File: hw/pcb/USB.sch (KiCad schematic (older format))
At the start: 9 parts, among them J301 USB_B_Micro, Q301 SS8050-G, Q302 SS8050-G, U301 CP2102N-A01-GQFN28

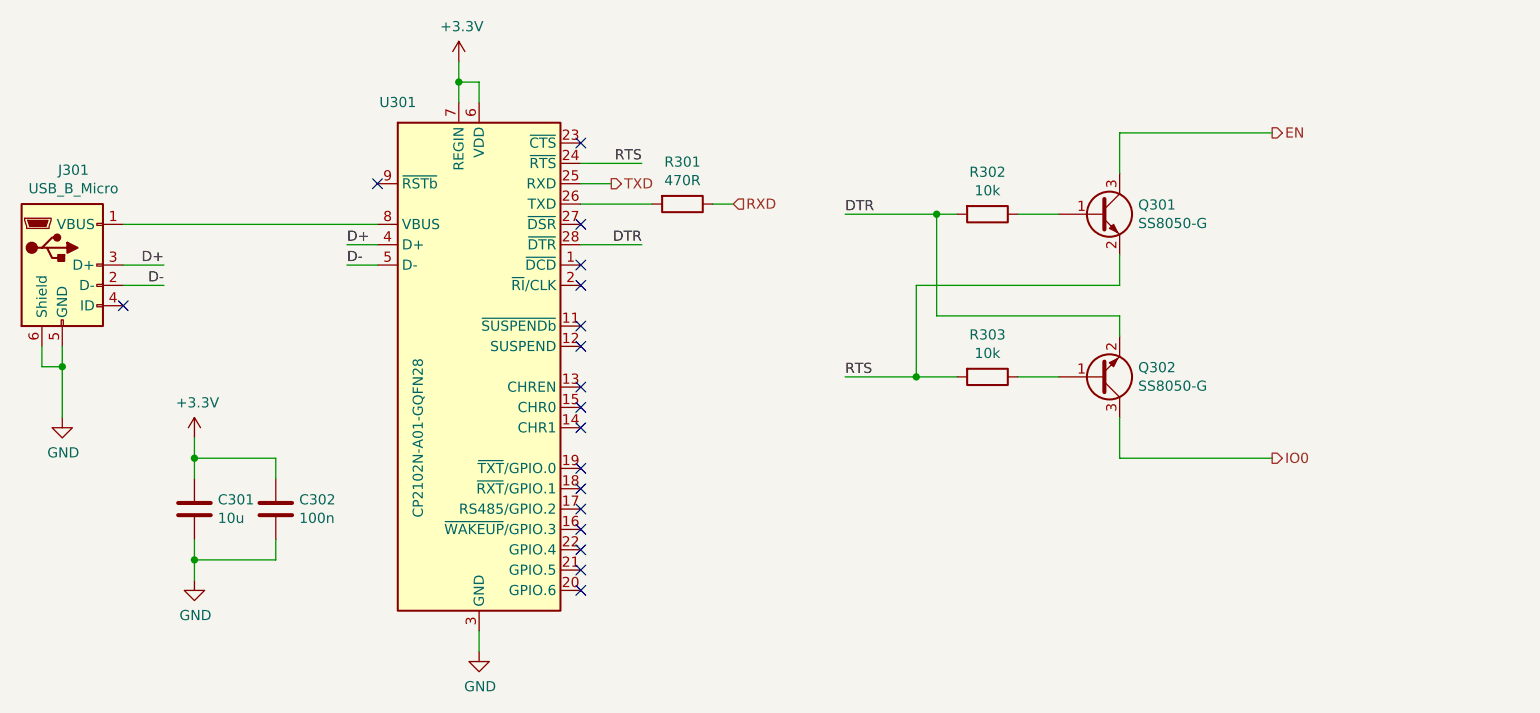
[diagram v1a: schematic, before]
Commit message: fixed severe PCB issue, clearance of ground fills was too small, could lead to thermal instability
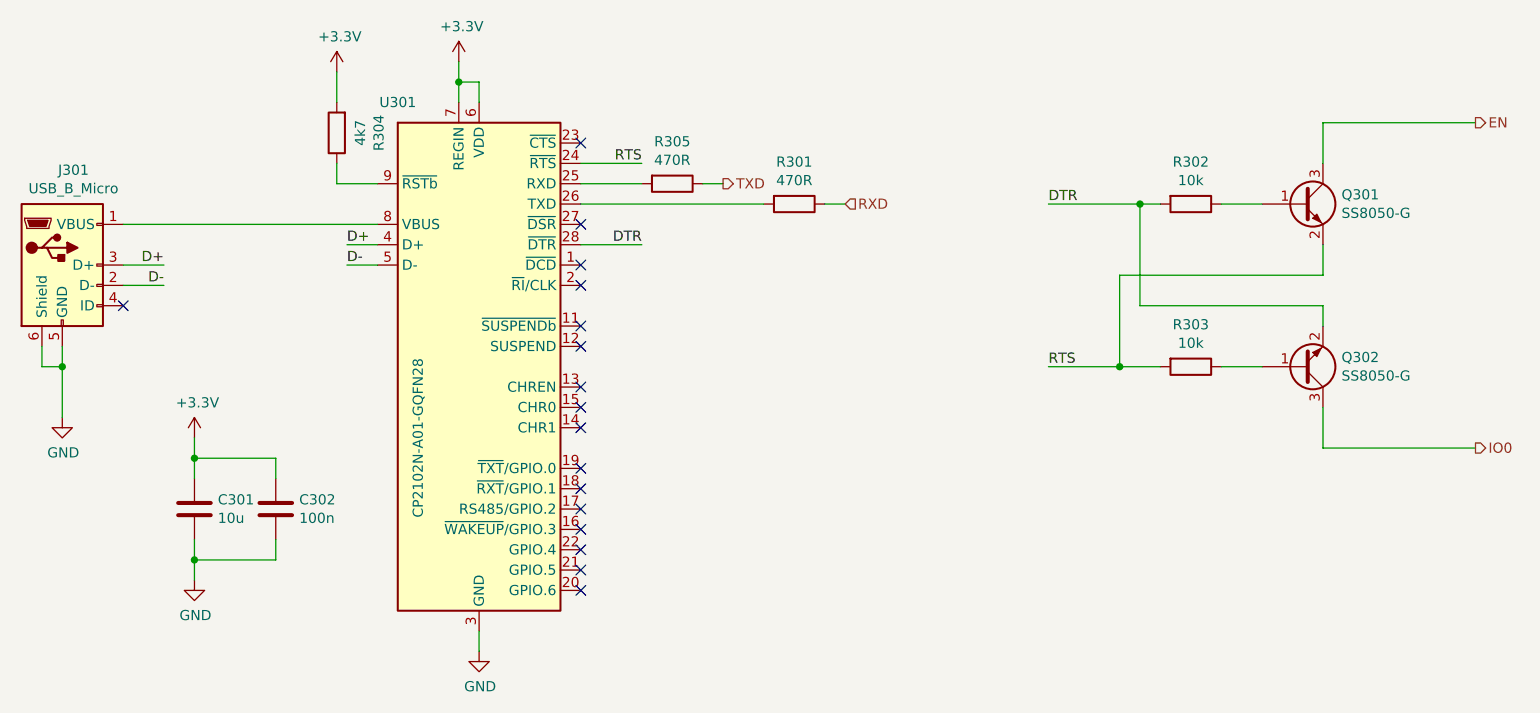
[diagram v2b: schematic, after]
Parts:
- added R304: 4k7, Resistor_SMD:R_0402_1005Metric, symbol Device:R
- added R305: 470R, Resistor_SMD:R_0402_1005Metric, symbol Device:R
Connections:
- net +3V3: now also R304.2
- net TXD: now also R305.1; no longer U301.25 (RXD)
- net at U301.9 (~RSTb): now also R304.1
- new net: R305.2, U301.25 (RXD)
- no-connect marks 18 -> 17
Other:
- moved on the sheet: Q301, Q302, R301, R302, R303
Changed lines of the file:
@@
 encoding utf-8
 Sheet 3 6
-Title "CTAG-TBD"
-Date "2020-06-06"
-Rev "C"
+Title "ESP32 Eurorack Audio Module"
+Date "2020-08-18"
+Rev "G"
 Comp "(c) Robert Manzke 2020"
 Comment1 "https://creativecommons.org/licenses/by-nc-sa/4.0/"
@@
 L Device:Q_NPN_BEC Q?
 U 1 1 5B81BF2F
-P 8150 1650
+P 9150 1600
 AR Path="/5B66F258/5B81BF2F" Ref="Q?"  Part="1"
 AR Path="/5B81850F/5B81BF2F" Ref="Q301"  Part="1"
-F 0 "Q301" H 8341 1696 50  0000 L CNN
-F 1 "SS8050-G" H 8341 1605 50  0000 L CNN
-F 2 "Package_TO_SOT_SMD:SOT-23" H 8350 1750 50  0001 C CNN
-F 3 "~" H 8150 1650 50  0001 C CNN
-	1    8150 1650
+F 0 "Q301" H 9341 1646 50  0000 L CNN
+F 1 "SS8050-G" H 9341 1555 50  0000 L CNN
+F 2 "Package_TO_SOT_SMD:SOT-23" H 9350 1700 50  0001 C CNN
+F 3 "~" H 9150 1600 50  0001 C CNN
+	1    9150 1600
 	1    0    0    -1
 $EndComp
@@
 L Device:Q_NPN_BEC Q?
 U 1 1 5B81BF36
-P 8150 2450
+P 9150 2400
 AR Path="/5B66F258/5B81BF36" Ref="Q?"  Part="1"
 AR Path="/5B81850F/5B81BF36" Ref="Q302"  Part="1"
-F 0 "Q302" H 8341 2404 50  0000 L CNN
-F 1 "SS8050-G" H 8341 2495 50  0000 L CNN
-F 2 "Package_TO_SOT_SMD:SOT-23" H 8350 2550 50  0001 C CNN
-F 3 "~" H 8150 2450 50  0001 C CNN
-	1    8150 2450
+F 0 "Q302" H 9341 2354 50  0000 L CNN
+F 1 "SS8050-G" H 9341 2445 50  0000 L CNN
+F 2 "Package_TO_SOT_SMD:SOT-23" H 9350 2500 50  0001 C CNN
+F 3 "~" H 9150 2400 50  0001 C CNN
+	1    9150 2400
 	1    0    0    1
 $EndComp
@@
 L Device:R R?
 U 1 1 5B81BF3D
-P 7600 1650
+P 8600 1600
 AR Path="/5B66F258/5B81BF3D" Ref="R?"  Part="1"
 AR Path="/5B81850F/5B81BF3D" Ref="R302"  Part="1"
-F 0 "R302" V 7393 1650 50  0000 C CNN
-F 1 "10k" V 7484 1650 50  0000 C CNN
-F 2 "Resistor_SMD:R_0402_1005Metric" V 7530 1650 50  0001 C CNN
-F 3 "~" H 7600 1650 50  0001 C CNN
-	1    7600 1650
+F 0 "R302" V 8393 1600 50  0000 C CNN
+F 1 "10k" V 8484 1600 50  0000 C CNN
+F 2 "Resistor_SMD:R_0402_1005Metric" V 8530 1600 50  0001 C CNN
+F 3 "~" H 8600 1600 50  0001 C CNN
+	1    8600 1600
 	0    1    1    0
 $EndComp
@@
 L Device:R R?
 U 1 1 5B81BF44
-P 7600 2450
+P 8600 2400
 AR Path="/5B66F258/5B81BF44" Ref="R?"  Part="1"
 AR Path="/5B81850F/5B81BF44" Ref="R303"  Part="1"
-F 0 "R303" V 7393 2450 50  0000 C CNN
-F 1 "10k" V 7484 2450 50  0000 C CNN
-F 2 "Resistor_SMD:R_0402_1005Metric" V 7530 2450 50  0001 C CNN
-F 3 "~" H 7600 2450 50  0001 C CNN
-	1    7600 2450
+F 0 "R303" V 8393 2400 50  0000 C CNN
+F 1 "10k" V 8484 2400 50  0000 C CNN
+F 2 "Resistor_SMD:R_0402_1005Metric" V 8530 2400 50  0001 C CNN
+F 3 "~" H 8600 2400 50  0001 C CNN
+	1    8600 2400
 	0    1    1    0
 $EndComp
 Wire Wire Line
-	7950 1650 7750 1650
-Wire Wire Line
-	7950 2450 7750 2450
-Wire Wire Line
-	8250 1850 8250 2000
-Wire Wire Line
-	8250 2000 7250 2000
-Wire Wire Line
-	7250 2000 7250 2450
-Wire Wire Line
-	7250 2450 7450 2450
-Wire Wire Line
-	8250 2250 8250 2150
-Wire Wire Line
-	7350 2150 7350 1650
-Wire Wire Line
-	7350 1650 7450 1650
-Wire Wire Line
-	8250 1250 8250 1450
-Wire Wire Line
-	8250 2650 8250 2850
-Connection ~ 7350 1650
-Wire Wire Line
-	7250 2450 6900 2450
-Connection ~ 7250 2450
-Text Label 6900 1650 0    50   ~ 0
+	8950 1600 8750 1600
+Wire Wire Line
+	8950 2400 8750 2400
+Wire Wire Line
+	9250 1800 9250 1950
+Wire Wire Line
+	9250 1950 8250 1950
+Wire Wire Line
+	8250 1950 8250 2400
+Wire Wire Line
+	8250 2400 8450 2400
+Wire Wire Line
+	9250 2200 9250 2100
+Wire Wire Line
+	8350 2100 8350 1600
+Wire Wire Line
+	8350 1600 8450 1600
+Wire Wire Line
+	9250 1200 9250 1400
+Wire Wire Line
+	9250 2600 9250 2800
+Connection ~ 8350 1600
+Wire Wire Line
+	8250 2400 7900 2400
+Connection ~ 8250 2400
+Text Label 7900 1600 0    50   ~ 0
 DTR
-Text Label 6900 2450 0    50   ~ 0
+Text Label 7900 2400 0    50   ~ 0
 RTS
 $Comp
@@
 Wire Wire Line
 	5600 1800 5900 1800
-Text HLabel 9000 1250 2    50   Output ~ 0
+Text HLabel 10000 1200 2    50   Output ~ 0
 EN
-Text HLabel 9000 2850 2    50   Output ~ 0
+Text HLabel 10000 2800 2    50   Output ~ 0
 IO0
-Text HLabel 5750 1500 2    50   Output ~ 0
+Text HLabel 6300 1500 2    50   Output ~ 0
 TXD
-Text HLabel 6350 1600 2    50   Input ~ 0
+Text HLabel 6900 1600 2    50   Input ~ 0
 RXD
 Wire Wire Line
 	5600 1400 5900 1400
 Wire Wire Line
-	5600 1500 5750 1500
-Wire Wire Line
-	8250 1250 9000 1250
-Wire Wire Line
-	6900 1650 7350 1650
-Wire Wire Line
-	8250 2850 9000 2850
+	9250 1200 10000 1200
+Wire Wire Line
+	7900 1600 8350 1600
+Wire Wire Line
+	9250 2800 10000 2800
 $Comp
 L Device:C C?
@@
 NoConn ~ 5600 3500
 Wire Wire Line
-	7350 2150 8250 2150
+	8350 2100 9250 2100
 NoConn ~ 3350 2100
 Wire Wire Line
@@
 Wire Wire Line
 	3050 2400 3050 2650
-NoConn ~ 4600 1500
 $Comp
 L Device:R R301
 U 1 1 5DBD0908
-P 6100 1600
-F 0 "R301" V 5893 1600 50  0000 C CNN
-F 1 "470R" V 5984 1600 50  0000 C CNN
-F 2 "Resistor_SMD:R_0402_1005Metric" V 6030 1600 50  0001 C CNN
-F 3 "~" H 6100 1600 50  0001 C CNN
-	1    6100 1600
+P 6650 1600
+F 0 "R301" V 6443 1600 50  0000 C CNN
+F 1 "470R" V 6534 1600 50  0000 C CNN
+F 2 "Resistor_SMD:R_0402_1005Metric" V 6580 1600 50  0001 C CNN
+F 3 "~" H 6650 1600 50  0001 C CNN
+	1    6650 1600
 	0    1    1    0
 $EndComp
 Wire Wire Line
-	5950 1600 5600 1600
-Wire Wire Line
-	6250 1600 6350 1600
+	6500 1600 5600 1600
+Wire Wire Line
+	6800 1600 6900 1600
 Wire Wire Line
 	3350 1700 4600 1700
+$Comp
+L Device:R R304
+U 1 1 5F132412
+P 4400 1250
+F 0 "R304" V 4193 1250 50  0000 C CNN
+F 1 "4k7" V 4284 1250 50  0000 C CNN
+F 2 "Resistor_SMD:R_0402_1005Metric" V 4330 1250 50  0001 C CNN
+F 3 "~" H 4400 1250 50  0001 C CNN
+	1    4400 1250
+	-1   0    0    1
+$EndComp
+Wire Wire Line
+	4600 1500 4400 1500
+Wire Wire Line
+	4400 1500 4400 1400
+$Comp
+L power:+3.3V #PWR?
+U 1 1 5F13365B
+P 4400 950
+AR Path="/5B66F258/5F13365B" Ref="#PWR?"  Part="1"
+AR Path="/5B81850F/5F13365B" Ref="#PWR0306"  Part="1"
+F 0 "#PWR0306" H 4400 800 50  0001 C CNN
+F 1 "+3.3V" H 4415 1123 50  0000 C CNN
+F 2 "" H 4400 950 50  0001 C CNN
+F 3 "" H 4400 950 50  0001 C CNN
+	1    4400 950
+	1    0    0    -1
+$EndComp
+Wire Wire Line
+	4400 950  4400 1100
+$Comp
+L Device:R R305
+U 1 1 5F14D379
+P 6050 1500
+F 0 "R305" V 5843 1500 50  0000 C CNN
+F 1 "470R" V 5934 1500 50  0000 C CNN
+F 2 "Resistor_SMD:R_0402_1005Metric" V 5980 1500 50  0001 C CNN
+F 3 "~" H 6050 1500 50  0001 C CNN
+	1    6050 1500
+	0    1    1    0
+$EndComp
+Wire Wire Line
+	6300 1500 6200 1500
+Wire Wire Line
+	5900 1500 5600 1500
 $EndSCHEMATC

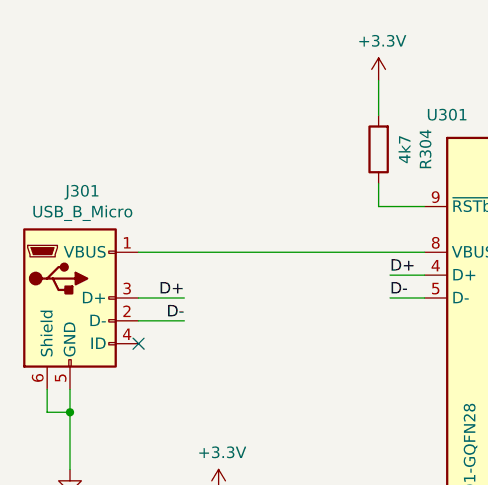
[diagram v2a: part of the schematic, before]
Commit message: Updated Eurorack hw to Rev. H
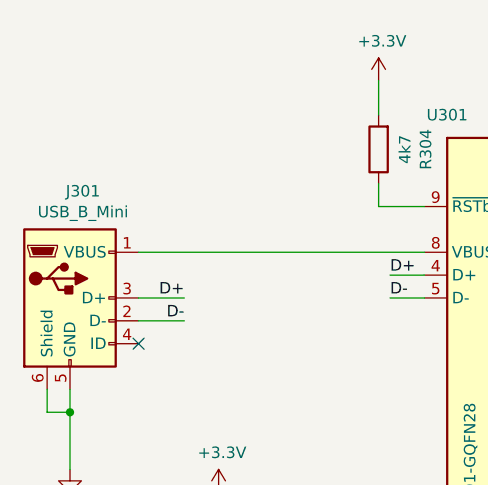
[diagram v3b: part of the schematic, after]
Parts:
- removed J301: USB_B_Micro, Connector_USB:USB_Micro-B_Molex-105017-0001, symbol Connector:USB_B_Micro
- added J301: USB_B_Mini, Connector_USB:USB_Mini-B_Tensility_54-00023_Vertical, symbol Connector:USB_B_Mini
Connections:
- net D+: now also J301.3 (D+)
- net D-: now also J301.2 (D-)
- net GND: now also J301.5 (GND), J301.6 (Shield)
- net at U301.8 (VBUS): now also J301.1 (VBUS)
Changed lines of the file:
@@
 Sheet 3 6
 Title "ESP32 Eurorack Audio Module"
-Date "2020-08-18"
-Rev "G"
-Comp "(c) Robert Manzke 2020"
+Date "2021-10-05"
+Rev "H"
+Comp "(c) Robert Manzke 2021"
 Comment1 "https://creativecommons.org/licenses/by-nc-sa/4.0/"
 Comment2 "Licensed under CC BY-NC-SA 4.0"
@@
 	3550 2000 3350 2000
 $Comp
-L Connector:USB_B_Micro J?
-U 1 1 5B81BF77
-P 3050 1900
-AR Path="/5B66F258/5B81BF77" Ref="J?"  Part="1"
-AR Path="/5B81850F/5B81BF77" Ref="J301"  Part="1"
-F 0 "J301" H 3105 2367 50  0000 C CNN
-F 1 "USB_B_Micro" H 3105 2276 50  0000 C CNN
-F 2 "Connector_USB:USB_Micro-B_Molex-105017-0001" H 3200 1850 50  0001 C CNN
-F 3 "~" H 3200 1850 50  0001 C CNN
-	1    3050 1900
-	1    0    0    -1
-$EndComp
-$Comp
 L power:GND #PWR?
 U 1 1 5B81BF7F
@@
 Wire Wire Line
 	5900 1500 5600 1500
+$Comp
+L Connector:USB_B_Mini J301
+U 1 1 615C2579
+P 3050 1900
+F 0 "J301" H 3107 2367 50  0000 C CNN
+F 1 "USB_B_Mini" H 3107 2276 50  0000 C CNN
+F 2 "Connector_USB:USB_Mini-B_Tensility_54-00023_Vertical" H 3200 1850 50  0001 C CNN
+F 3 "~" H 3200 1850 50  0001 C CNN
+	1    3050 1900
+	1    0    0    -1
+$EndComp
 $EndSCHEMATC
